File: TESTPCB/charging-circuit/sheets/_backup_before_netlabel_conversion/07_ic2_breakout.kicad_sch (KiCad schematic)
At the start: 2 parts, among them U5 BQ25606RGER, U7 Z-21320110021001

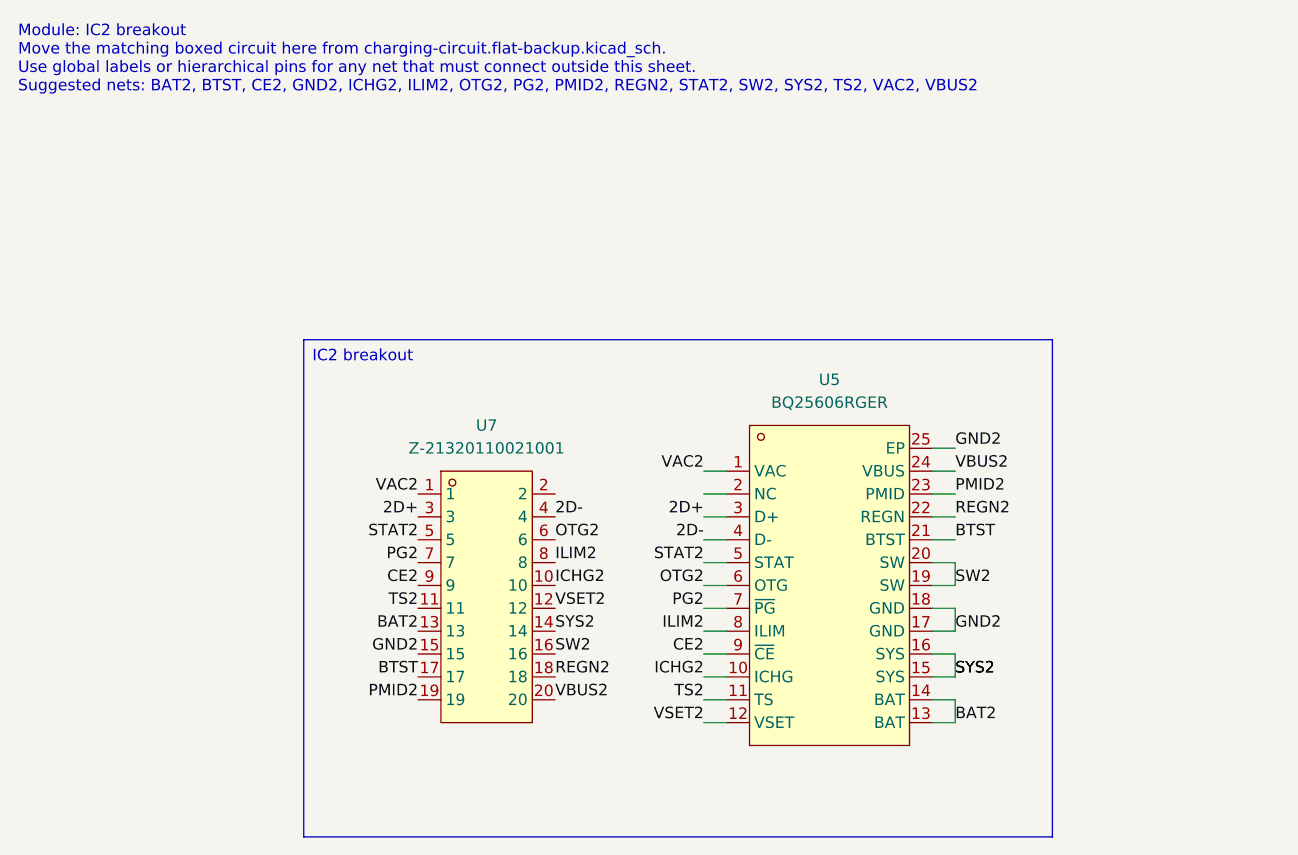
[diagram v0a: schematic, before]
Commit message: Fixed formatting issues, now the hierachal sheets are all labeled as net labels and when we want to expose their pins we will make them into hierchal or global pins
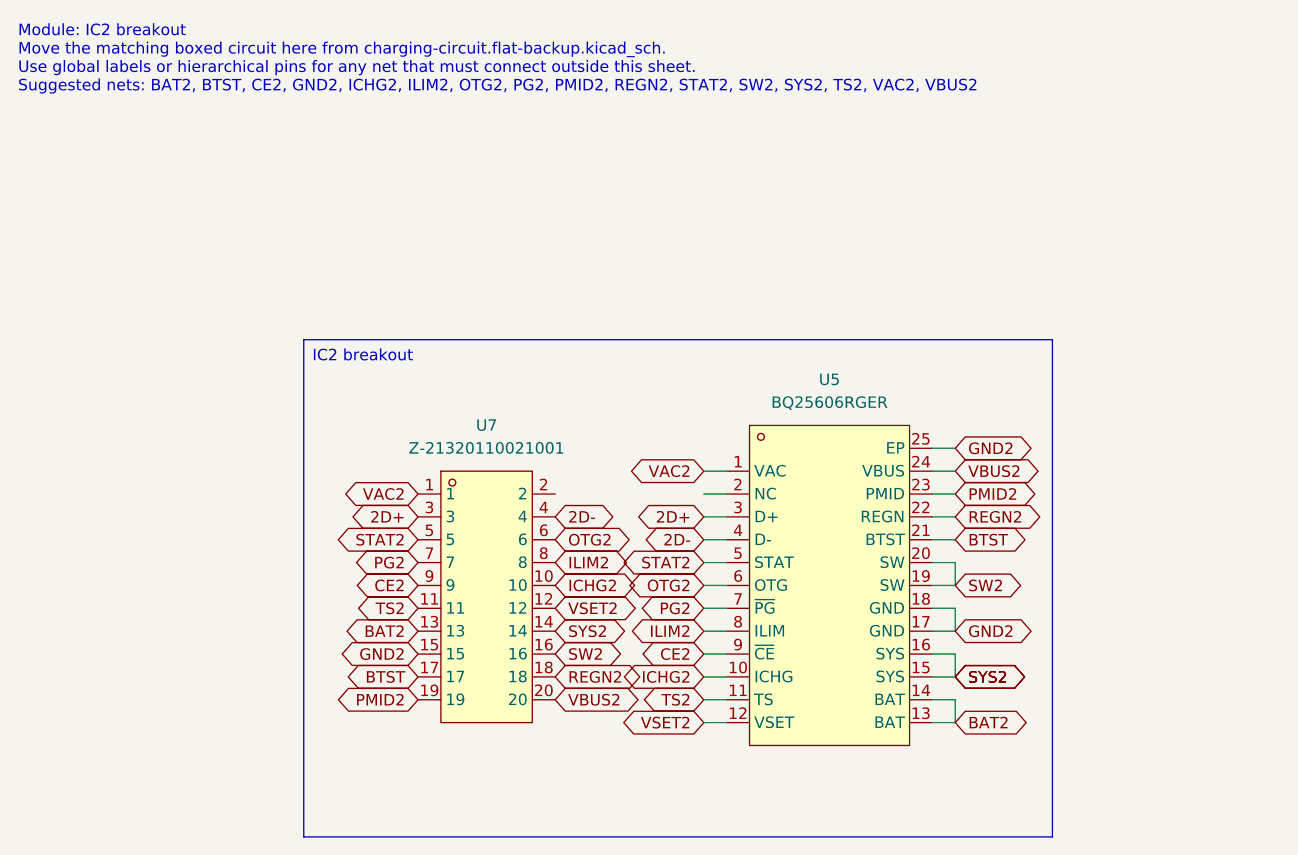
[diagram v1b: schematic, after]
